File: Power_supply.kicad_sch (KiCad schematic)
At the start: 47 parts, among them J1 Transformers, J20 HV_Transformer, J21 LV_Transformer, J22 220V, J23 Transformers, J25 Anodes_enable, J26 Conn_01x04, J27 Conn_01x04, J28 Conn_01x04, Q1 STP4NK60ZFP(MJE13003)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

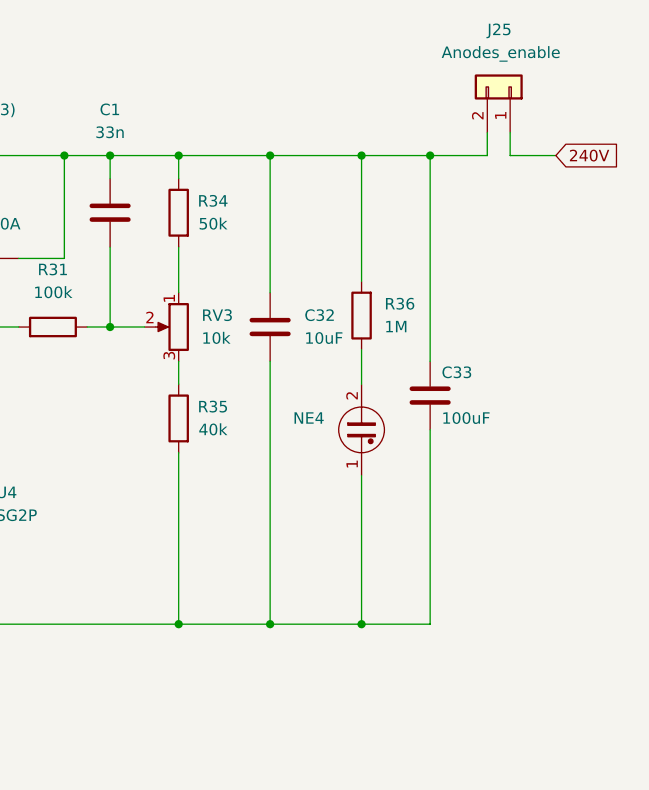
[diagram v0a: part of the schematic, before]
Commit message: Continue rebuilding power supply PCB
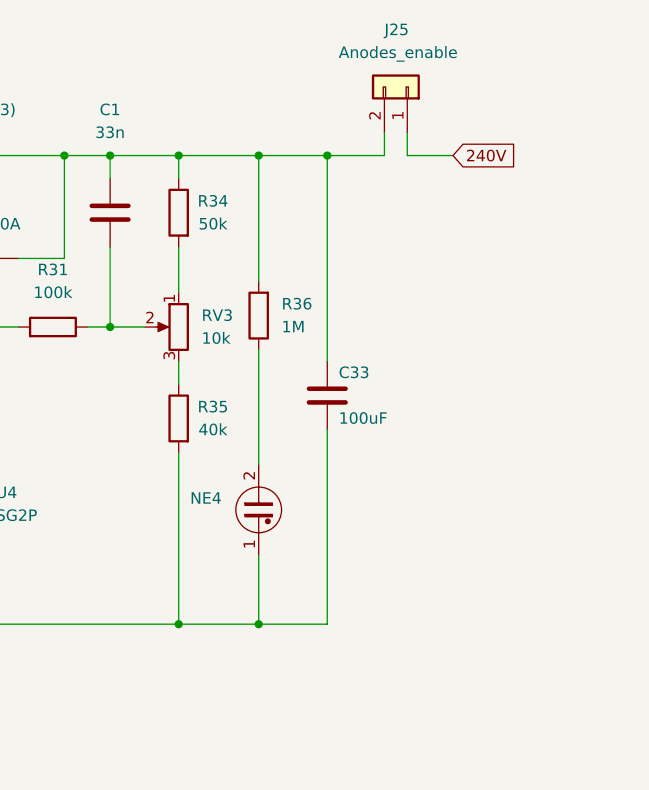
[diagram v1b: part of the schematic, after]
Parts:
- removed C32: 10uF, spdf1626_lib:C_THT_D10.0mm_P5.00mm, symbol Device:C
- C25: footprint Capacitor_THT:CP_Radial_D6.3mm_P2.50mm -> spdf1626_lib:C_THT_D13mm_P5.08mm
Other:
- moved on the sheet: C33, J25, NE4, R36

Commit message: PCB almost done
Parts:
- removed C27: 100n, spdf1626_lib:C_THT_K73-17_P9.00mm, symbol Device:C
- removed J26, J27, J28: Conn_01x04, spdf1626_lib:PinHeader_1x04_P2.54mm, symbol Connector_Generic:Conn_01x04
- added J2: 240V, spdf1626_lib:Connector_1x02_P5mm_Vertical, symbol Connector_Generic:Conn_01x02
- added J3: 6V3, spdf1626_lib:Connector_1x02_P5mm_Vertical, symbol Connector_Generic:Conn_01x02
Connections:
- net +6V: now also J3.1 (Pin_1)
- net 240V: now also J2.1 (Pin_1)
- net GND: now also J2.2 (Pin_2), J3.2 (Pin_2)
- net at R35.1: now also RV3.1; no longer RV3.3
- net at R34.2: now also RV3.3; no longer RV3.1
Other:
- moved on the sheet: RV3

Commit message: Rounded corners for power supply PCB
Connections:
- net 240V: now also J2.2 (Pin_2); no longer J2.1 (Pin_1)
- net GND: now also J2.1 (Pin_1); no longer J2.2 (Pin_2)
- net at L2.1: now also J22.2 (Pin_2); no longer J22.1 (Pin_1)
- net at L2.4: now also J22.1 (Pin_1); no longer J22.2 (Pin_2)
- net at R35.1: now also RV3.3; no longer RV3.1
- net at R34.2: now also RV3.1; no longer RV3.3
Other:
- moved on the sheet: J22, RV3
